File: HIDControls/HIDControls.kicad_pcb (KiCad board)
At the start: 2 copper layers, 83.8 x 91.4 mm, 70 parts, among them M1 ModulePlug, M10 ModulePlug, M11 ModulePlug, M12 ModulePlug, M2 ModulePlug, M3 ModulePlug, M4 ModulePlug, M5 ModulePlug, M6 ModulePlug, M7 ModulePlug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

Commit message: Minor layout tweaks
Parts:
- R14: moved to B.Cu
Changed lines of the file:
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@@
     (property "Sheetname" "")
     (attr through_hole)
-    (fp_text reference "SW5" (at 7.55 2.44 180) (layer "F.SilkS")
+    (fp_text reference "SW5" (at 11.412 2.406) (layer "F.SilkS")
       (effects (font (size 1 1) (thickness 0.15)))
     )
@@
     )
   )
-  (footprint "Resistor_THT:R_Axial_DIN0207_L6.3mm_D2.5mm_P7.62mm_Horizontal" (layer "F.Cu")
-    (at 154.94 125.222)
-    (descr "Resistor, Axial_DIN0207 series, Axial, Horizontal, pin pitch=7.62mm, 0.25W = 1/4W, length*diameter=6.3*2.5mm^2, http://cdn-reichelt.de/documents/datenblatt/B400/1_4W%23YAG.pdf")
-    (tags "Resistor Axial_DIN0207 series Axial Horizontal pin pitch 7.62mm 0.25W = 1/4W length 6.3mm diameter 2.5mm")
-    (property "Sheetfile" "HIDControls.kicad_sch")
-    (property "Sheetname" "")
-    (attr through_hole)
-    (fp_text reference "R14" (at 3.81 0) (layer "F.SilkS")
-      (effects (font (size 1 1) (thickness 0.15)))
-    )
-    (fp_text value "10k" (at 3.81 2.37) (layer "F.Fab")
-      (effects (font (size 1 1) (thickness 0.15)))
-    )
-    (fp_text user "${REFERENCE}" (at 3.81 0) (layer "F.Fab")
-      (effects (font (size 1 1) (thickness 0.15)))
-    )
-    (fp_line (start 0.54 1.37) (end 7.08 1.37) (layer "F.SilkS") (width 0.12))
-    (fp_line (start 0.54 -1.04) (end 0.54 -1.37) (layer "F.SilkS") (width 0.12))
-    (fp_line (start 0.54 1.04) (end 0.54 1.37) (layer "F.SilkS") (width 0.12))
-    (fp_line (start 0.54 -1.37) (end 7.08 -1.37) (layer "F.SilkS") (width 0.12))
-    (fp_line (start 7.08 -1.37) (end 7.08 -1.04) (layer "F.SilkS") (width 0.12))
-    (fp_line (start 7.08 1.37) (end 7.08 1.04) (layer "F.SilkS") (width 0.12))
-    (fp_line (start -1.05 1.5) (end 8.67 1.5) (layer "F.CrtYd") (width 0.05))
-    (fp_line (start -1.05 -1.5) (end -1.05 1.5) (layer "F.CrtYd") (width 0.05))
-    (fp_line (start 8.67 -1.5) (end -1.05 -1.5) (layer "F.CrtYd") (width 0.05))
-    (fp_line (start 8.67 1.5) (end 8.67 -1.5) (layer "F.CrtYd") (width 0.05))
-    (fp_line (start 0.66 -1.25) (end 0.66 1.25) (layer "F.Fab") (width 0.1))
-    (fp_line (start 6.96 -1.25) (end 0.66 -1.25) (layer "F.Fab") (width 0.1))
-    (fp_line (start 6.96 1.25) (end 6.96 -1.25) (layer "F.Fab") (width 0.1))
-    (fp_line (start 0 0) (end 0.66 0) (layer "F.Fab") (width 0.1))
-    (fp_line (start 7.62 0) (end 6.96 0) (layer "F.Fab") (width 0.1))
-    (fp_line (start 0.66 1.25) (end 6.96 1.25) (layer "F.Fab") (width 0.1))
-    (pad "1" thru_hole circle (at 0 0) (size 1.6 1.6) (drill 0.8) (layers *.Cu *.Mask)
-      (net 70 "Net-(M11-Pad4)") (pintype "passive"))
-    (pad "2" thru_hole oval (at 7.62 0) (size 1.6 1.6) (drill 0.8) (layers *.Cu *.Mask)
-      (net 69 "Net-(M11-Pad3)") (pintype "passive"))
-    (model "${KICAD6_3DMODEL_DIR}/Resistor_THT.3dshapes/R_Axial_DIN0207_L6.3mm_D2.5mm_P7.62mm_Horizontal.wrl"
-      (offset (xyz 0 0 0))
-      (scale (xyz 1 1 1))
-      (rotate (xyz 0 0 0))
-    )
-  )
   (footprint "HIDControls:ModulePlug" (layer "F.Cu")
     (at 130.81 87.63)
@@
     (model "${KICAD6_3DMODEL_DIR}/Resistor_THT.3dshapes/R_Axial_DIN0207_L6.3mm_D2.5mm_P7.62mm_Horizontal.wrl"
       (offset (xyz 0 0 0))
+      (scale (xyz 1 1 1))
+      (rotate (xyz 0 0 0))
+    )
+  )
+  (footprint "Resistor_THT:R_Axial_DIN0207_L6.3mm_D2.5mm_P7.62mm_Horizontal" (layer "B.Cu")
+    (at 154.94 125.222)
+    (descr "Resistor, Axial_DIN0207 series, Axial, Horizontal, pin pitch=7.62mm, 0.25W = 1/4W, length*diameter=6.3*2.5mm^2, http://cdn-reichelt.de/documents/datenblatt/B400/1_4W%23YAG.pdf")
+    (tags "Resistor Axial_DIN0207 series Axial Horizontal pin pitch 7.62mm 0.25W = 1/4W length 6.3mm diameter 2.5mm")
+    (property "Sheetfile" "HIDControls.kicad_sch")
+    (property "Sheetname" "")
+    (attr through_hole)
+    (fp_text reference "R14" (at 3.81 0) (layer "B.SilkS")
+      (effects (font (size 1 1) (thickness 0.15)) (justify mirror))
+    )
+    (fp_text value "10k" (at 3.81 -2.37) (layer "B.Fab")
+      (effects (font (size 1 1) (thickness 0.15)) (justify mirror))
+    )
+    (fp_text user "${REFERENCE}" (at 3.81 0) (layer "B.Fab")
+      (effects (font (size 1 1) (thickness 0.15)) (justify mirror))
+    )
+    (fp_line (start 0.54 -1.37) (end 7.08 -1.37) (layer "B.SilkS") (width 0.12))
+    (fp_line (start 0.54 1.04) (end 0.54 1.37) (layer "B.SilkS") (width 0.12))
+    (fp_line (start 0.54 -1.04) (end 0.54 -1.37) (layer "B.SilkS") (width 0.12))
+    (fp_line (start 0.54 1.37) (end 7.08 1.37) (layer "B.SilkS") (width 0.12))
+    (fp_line (start 7.08 1.37) (end 7.08 1.04) (layer "B.SilkS") (width 0.12))
+    (fp_line (start 7.08 -1.37) (end 7.08 -1.04) (layer "B.SilkS") (width 0.12))
+    (fp_line (start -1.05 -1.5) (end 8.67 -1.5) (layer "B.CrtYd") (width 0.05))
+    (fp_line (start -1.05 1.5) (end -1.05 -1.5) (layer "B.CrtYd") (width 0.05))
+    (fp_line (start 8.67 1.5) (end -1.05 1.5) (layer "B.CrtYd") (width 0.05))
+    (fp_line (start 8.67 -1.5) (end 8.67 1.5) (layer "B.CrtYd") (width 0.05))
+    (fp_line (start 0.66 1.25) (end 0.66 -1.25) (layer "B.Fab") (width 0.1))
+    (fp_line (start 6.96 1.25) (end 0.66 1.25) (layer "B.Fab") (width 0.1))
+    (fp_line (start 6.96 -1.25) (end 6.96 1.25) (layer "B.Fab") (width 0.1))
+    (fp_line (start 0 0) (end 0.66 0) (layer "B.Fab") (width 0.1))
+    (fp_line (start 7.62 0) (end 6.96 0) (layer "B.Fab") (width 0.1))
+    (fp_line (start 0.66 -1.25) (end 6.96 -1.25) (layer "B.Fab") (width 0.1))
+    (pad "1" thru_hole circle (at 0 0) (size 1.6 1.6) (drill 0.8) (layers *.Cu *.Mask)
+      (net 70 "Net-(M11-Pad4)") (pintype "passive"))
+    (pad "2" thru_hole oval (at 7.62 0) (size 1.6 1.6) (drill 0.8) (layers *.Cu *.Mask)
+      (net 69 "Net-(M11-Pad3)") (pintype "passive"))
+    (model "${KICAD6_3DMODEL_DIR}/Resistor_THT.3dshapes/R_Axial_DIN0207_L6.3mm_D2.5mm_P7.62mm_Horizontal.wrl"
+      (offset (xyz 0 0 0))

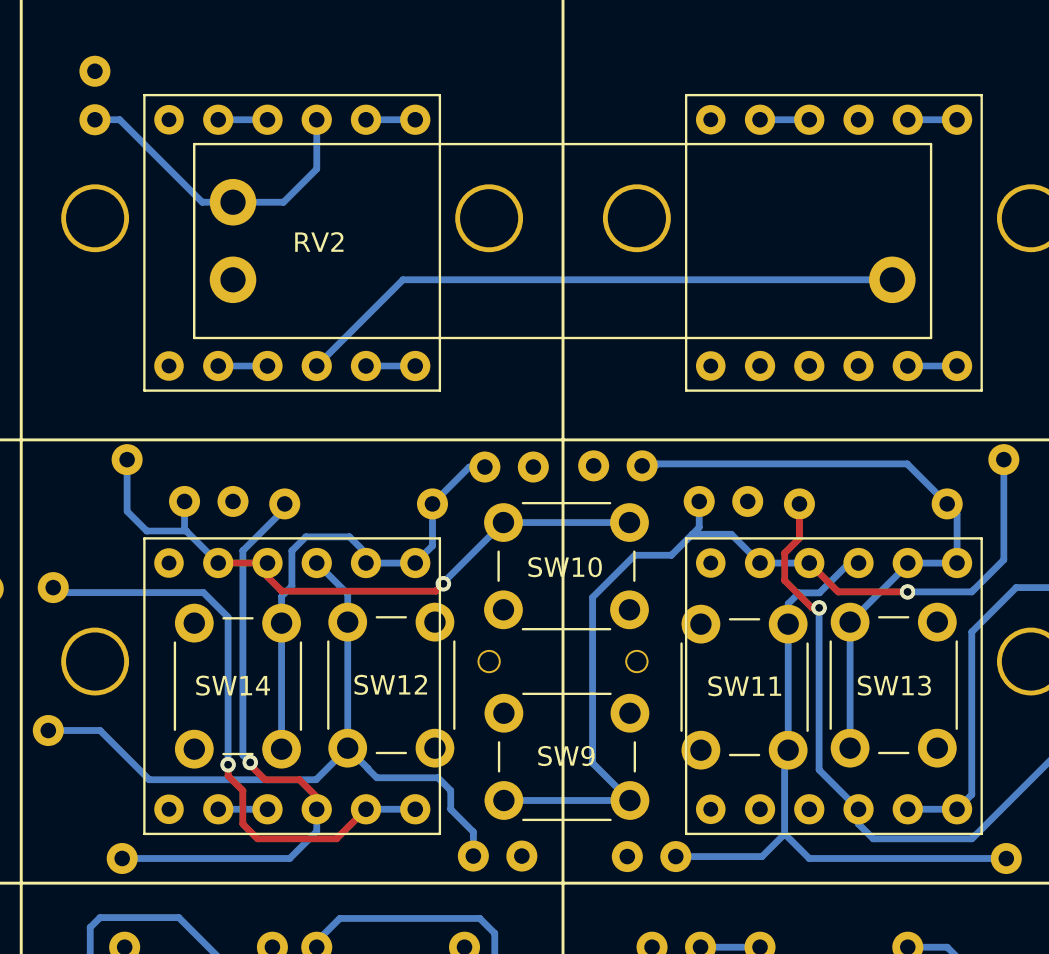
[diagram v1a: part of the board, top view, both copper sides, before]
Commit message: Added AnalogJoystick
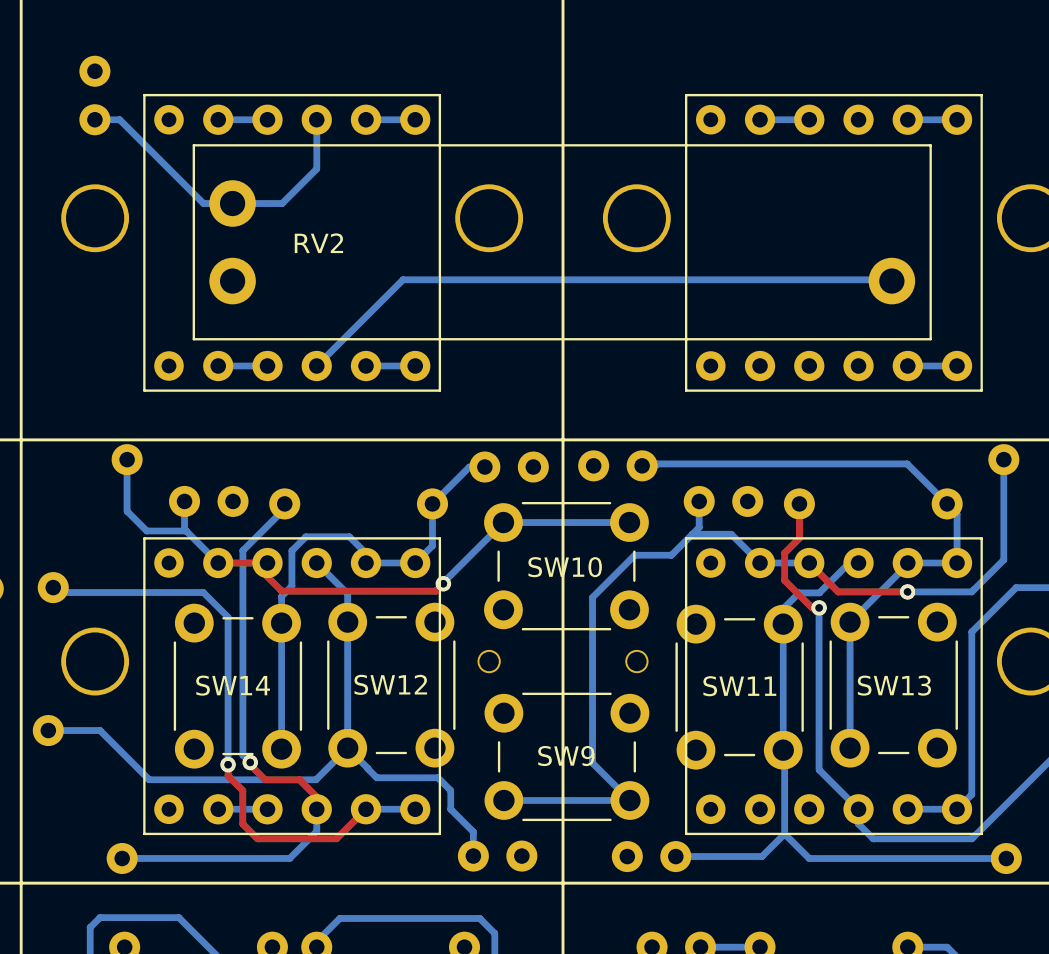
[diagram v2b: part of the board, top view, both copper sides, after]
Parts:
- moved SW11 0.25 mm to (151.6, 115.1)
- moved RV2 0.07 mm to (127.7, 90.9)
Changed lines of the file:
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@@
   )
   (footprint "Button_Switch_THT:SW_PUSH_6mm" (layer "F.Cu")
-    (at 151.892 115.062 90)
+    (at 151.638 115.062 90)
     (descr "https://www.omron.com/ecb/products/pdf/en-b3f.pdf")
     (tags "tact sw push 6mm")
@@
   )
   (footprint "HIDPanel:Linear-Pot-2031N" (layer "F.Cu")
-    (at 127.762 90.805)
+    (at 127.74 90.87)
     (property "Sheetfile" "HIDControls.kicad_sch")
     (property "Sheetname" "")
@@
   (segment (start 164.592 68.326) (end 164.592 64.008) (width 0.35) (layer "B.Cu") (net 62))
   (segment (start 160.02 59.69) (end 160.02 61.81) (width 0.35) (layer "B.Cu") (net 62))
-  (segment (start 130.365 86.805) (end 132.08 85.09) (width 0.35) (layer "B.Cu") (net 63))
-  (segment (start 121.92 82.55) (end 126.175 86.805) (width 0.35) (layer "B.Cu") (net 63))
-  (segment (start 127.762 86.805) (end 130.365 86.805) (width 0.35) (layer "B.Cu") (net 63))
+  (segment (start 126.24 86.87) (end 127.74 86.87) (width 0.35) (layer "B.Cu") (net 63))
+  (segment (start 121.92 82.55) (end 126.24 86.87) (width 0.35) (layer "B.Cu") (net 63))
+  (segment (start 130.3 86.87) (end 132.08 85.09) (width 0.35) (layer "B.Cu") (net 63))
   (segment (start 132.08 85.09) (end 132.08 82.55) (width 0.35) (layer "B.Cu") (net 63))
+  (segment (start 127.74 86.87) (end 130.3 86.87) (width 0.35) (layer "B.Cu") (net 63))
   (segment (start 120.64 82.55) (end 121.92 82.55) (width 0.35) (layer "B.Cu") (net 63))
-  (segment (start 126.175 86.805) (end 127.762 86.805) (width 0.35) (layer "B.Cu") (net 63))
+  (segment (start 161.675 90.805) (end 136.525 90.805) (width 0.35) (layer "B.Cu") (net 64))
   (segment (start 136.525 90.805) (end 132.08 95.25) (width 0.35) (layer "B.Cu") (net 64))
-  (segment (start 161.762 90.805) (end 136.525 90.805) (width 0.35) (layer "B.Cu") (net 64))
+  (segment (start 161.74 90.87) (end 161.675 90.805) (width 0.35) (layer "B.Cu") (net 64))
   (segment (start 137.668 137.922) (end 138.6 138.854) (width 0.35) (layer "B.Cu") (net 65))
   (segment (start 139.7 125.222) (end 139.7 128.524) (width 0.35) (layer "B.Cu") (net 65))
@@
   (segment (start 122.301 102.743) (end 122.301 100.078443) (width 0.35) (layer "B.Cu") (net 78))
   (segment (start 167.64 120.65) (end 157.48 120.65) (width 0.35) (layer "B.Cu") (net 79))
-  (segment (start 156.956 106.95) (end 156.392 107.514) (width 0.35) (layer "B.Cu") (net 79))
+  (segment (start 156.138 108.562) (end 156.138 115.062) (width 0.35) (layer "B.Cu") (net 79))
   (segment (start 157.48 120.65) (end 156.21 119.38) (width 0.35) (layer "B.Cu") (net 79))
-  (segment (start 156.392 107.514) (end 156.392 108.562) (width 0.35) (layer "B.Cu") (net 79))
-  (segment (start 156.21 115.244) (end 156.392 115.062) (width 0.35) (layer "B.Cu") (net 79))
-  (segment (start 156.21 119.38) (end 156.21 115.244) (width 0.35) (layer "B.Cu") (net 79))
+  (segment (start 160.02 105.41) (end 159.544 105.41) (width 0.35) (layer "B.Cu") (net 79))
+  (segment (start 156.21 115.134) (end 156.138 115.062) (width 0.35) (layer "B.Cu") (net 79))
+  (segment (start 156.138 107.768) (end 156.138 108.562) (width 0.35) (layer "B.Cu") (net 79))
   (segment (start 155.0416 120.5484) (end 156.21 119.38) (width 0.35) (layer "B.Cu") (net 79))
+  (segment (start 158.004 106.95) (end 156.956 106.95) (width 0.35) (layer "B.Cu") (net 79))
   (segment (start 150.5966 120.5484) (end 155.0416 120.5484) (width 0.35) (layer "B.Cu") (net 79))
-  (segment (start 160.02 105.41) (end 159.544 105.41) (width 0.35) (layer "B.Cu") (net 79))
-  (segment (start 158.004 106.95) (end 156.956 106.95) (width 0.35) (layer "B.Cu") (net 79))
   (segment (start 159.544 105.41) (end 158.004 106.95) (width 0.35) (layer "B.Cu") (net 79))
-  (segment (start 156.392 108.562) (end 156.392 115.062) (width 0.35) (layer "B.Cu") (net 79))
+  (segment (start 156.21 119.38) (end 156.21 115.134) (width 0.35) (layer "B.Cu") (net 79))
+  (segment (start 156.956 106.95) (end 156.138 107.768) (width 0.35) (layer "B.Cu") (net 79))
   (segment (start 118.237 114.048444) (end 120.906444 114.048444) (width 0.35) (layer "B.Cu") (net 80))
   (segment (start 134.7216 116.0036) (end 133.676 114.958) (width 0.35) (layer "B.Cu") (net 80))

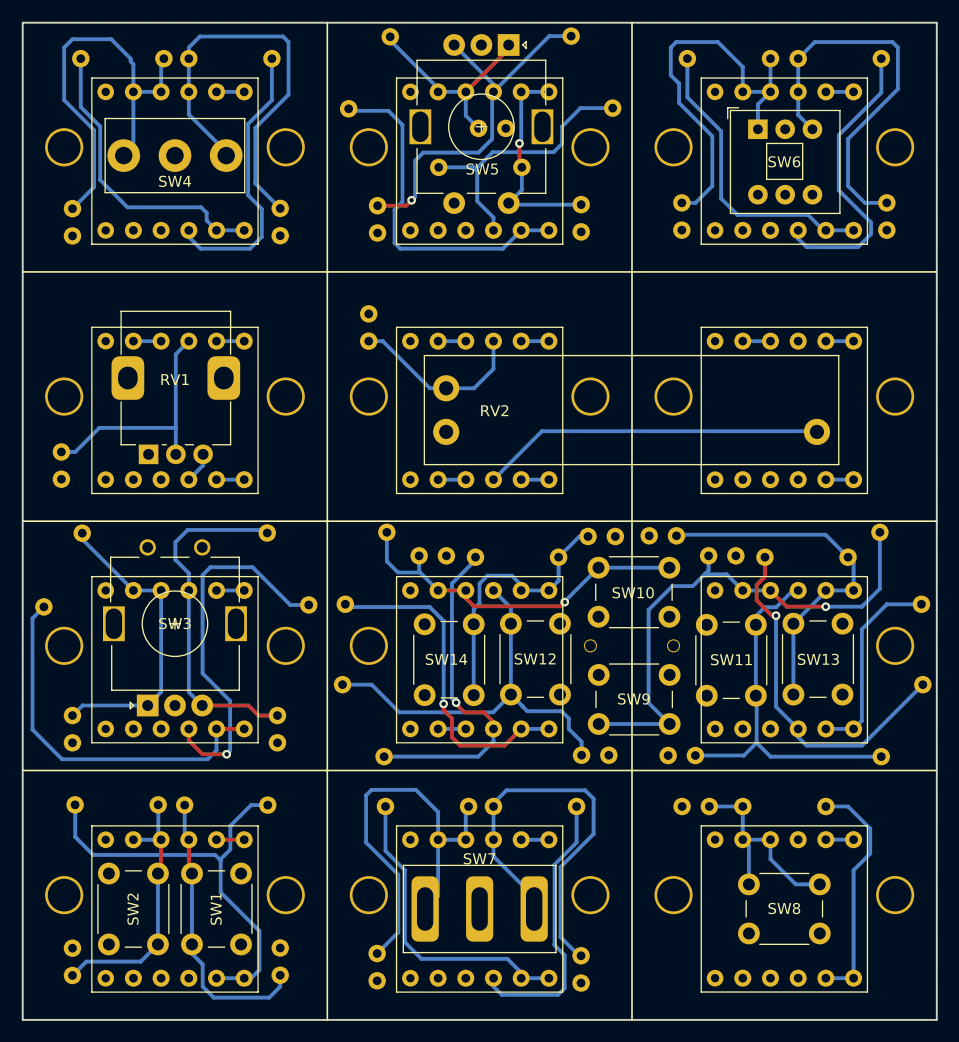
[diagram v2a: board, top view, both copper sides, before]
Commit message: Added analog joystick device
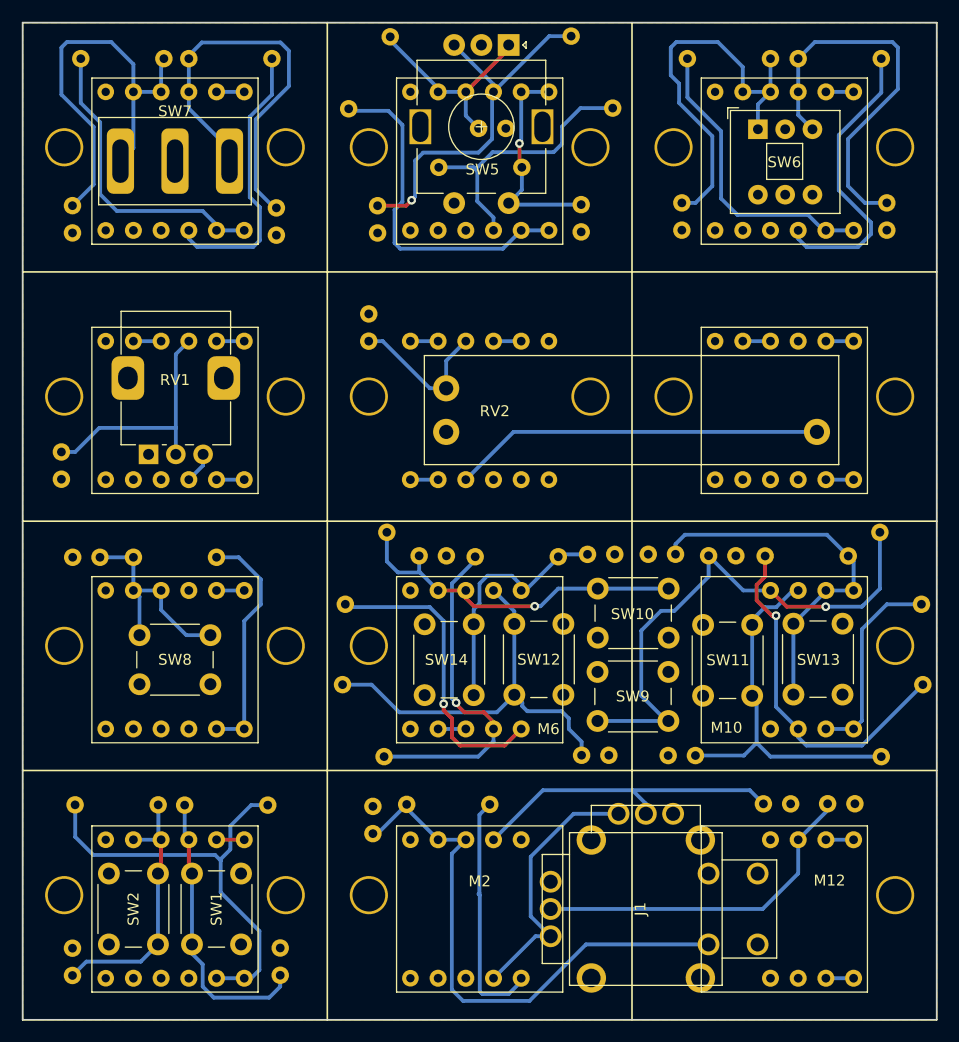
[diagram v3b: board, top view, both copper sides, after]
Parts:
- removed C11: 100 nF, Capacitor_THT:C_Disc_D5.0mm_W2.5mm_P2.50mm
- removed R4, R5, R6: 10k, Resistor_THT:R_Axial_DIN0207_L6.3mm_D2.5mm_P7.62mm_Horizontal
- removed SW3: ALPS EC11, Rotary_Encoder:RotaryEncoder_Alps_EC11E_Vertical_H20mm
- removed SW4: SS12D10, HIDPanel:SS12D10
- added J1: AnalogJoystick, HIDControls:AnalogJoystick, F.Cu at (146.1, 134.6)
- M10, M12: footprint HIDControls:ModulePlug -> HIDControls:RightPartModulePlug
- M2, M6: footprint HIDControls:ModulePlug -> HIDControls:LeftPartModulePlug
- M5: moved to B.Cu
- SW7: value 5mm TOGGLE -> 5mm TOGGLE, SS12D10
- moved M12 88.5 mm to (158.8, 133.3)
- moved C3 82.0 mm to (156.8, 125.0), turned to 0 degrees
- moved C14 74.1 mm to (93.5, 72.6)
- moved C13 74.1 mm to (112.2, 72.8)
- moved M7 74.1 mm to (102.9, 64.8)
- moved SW7 74.1 mm to (102.9, 66.0)
- moved R12 74.1 mm to (101.9, 56.6)
- moved R13 74.1 mm to (104.1, 56.6)
- moved C9 60.4 mm to (93.5, 102.4)
- moved M11 60.4 mm to (102.9, 110.5)
- moved R14 60.4 mm to (99.1, 102.4)
- moved SW8 60.4 mm to (106.1, 114.0)
- moved C10 53.2 mm to (165.2, 125.0), turned to 180 degrees
- moved C4 53.0 mm to (121.0, 125.2), turned to -90 degrees
- moved M2 36.1 mm to (130.8, 133.3)
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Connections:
- C10 pad 2: Net-(SW3-PadB) -> Net-(M12-Pad5)
- C3 pad 1: GND -> Net-(J1-Pad2)
- C3 pad 2: Net-(M12-Pad4) -> GND
- C4 pad 2: Net-(M12-Pad5) -> Net-(J1-PadA1)
- M12 pad 2: Net-(M12-Pad2) -> unconnected-(M12-Pad2)
- M12 pad 3: Net-(M12-Pad3) -> unconnected-(M12-Pad3)
- M12 pad 4: Net-(M12-Pad4) -> unconnected-(M12-Pad4)
- M2 pad 2: Net-(R3-Pad1) -> Net-(J1-Pad3)
- M2 pad 3: Net-(R4-Pad1) -> Net-(R3-Pad1)
- M2 pad 4: Net-(SW3-PadA) -> Net-(J1-PadA1)
- M2 pad 5: Net-(SW3-PadB) -> Net-(J1-Pad2)
- R3 pad 2: Net-(SW3-PadB) -> Net-(J1-PadA1)
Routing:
- net Net-(J1-PadA1): track 0.00 -> 51.6 mm
- net Net-(M12-Pad4): track 38.9 -> 0.00 mm
- net Net-(R4-Pad1): track 34.5 -> 0.00 mm
- net Net-(SW3-PadB): track 32.3 -> 0.00 mm
- net Net-(J1-Pad2): track 0.00 -> 29.8 mm
- net Net-(SW3-PadA): track 28.1 -> 0.00 mm
- net Net-(M12-Pad3): track 27.4 -> 0.00 mm
- net Net-(M12-Pad2): track 26.0 -> 0.00 mm
- net Net-(J1-Pad3): track 0.00 -> 24.6 mm
- net Net-(R3-Pad1): track 34.1 -> 22.3 mm, vias 1 -> 0
- net Net-(M12-Pad5): track 38.6 -> 31.6 mm
- net Net-(C2-Pad2): track 16.5 -> 14.0 mm
- net unconnected-(M2-Pad6): track 2.54 -> 0.00 mm
- net unconnected-(M12-Pad3): track 0.00 -> 2.54 mm
- net Net-(M6-Pad3): track 30.5 -> 27.9 mm
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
